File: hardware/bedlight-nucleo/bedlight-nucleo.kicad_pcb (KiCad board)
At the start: 2 copper layers, 76 x 76 mm, 18 parts, among them SW1 SW_Push, SW2 SW_Push, SW3 SW_Push, SW4 SW_Push, U1 Nucleo-32, U2 ULN2003A

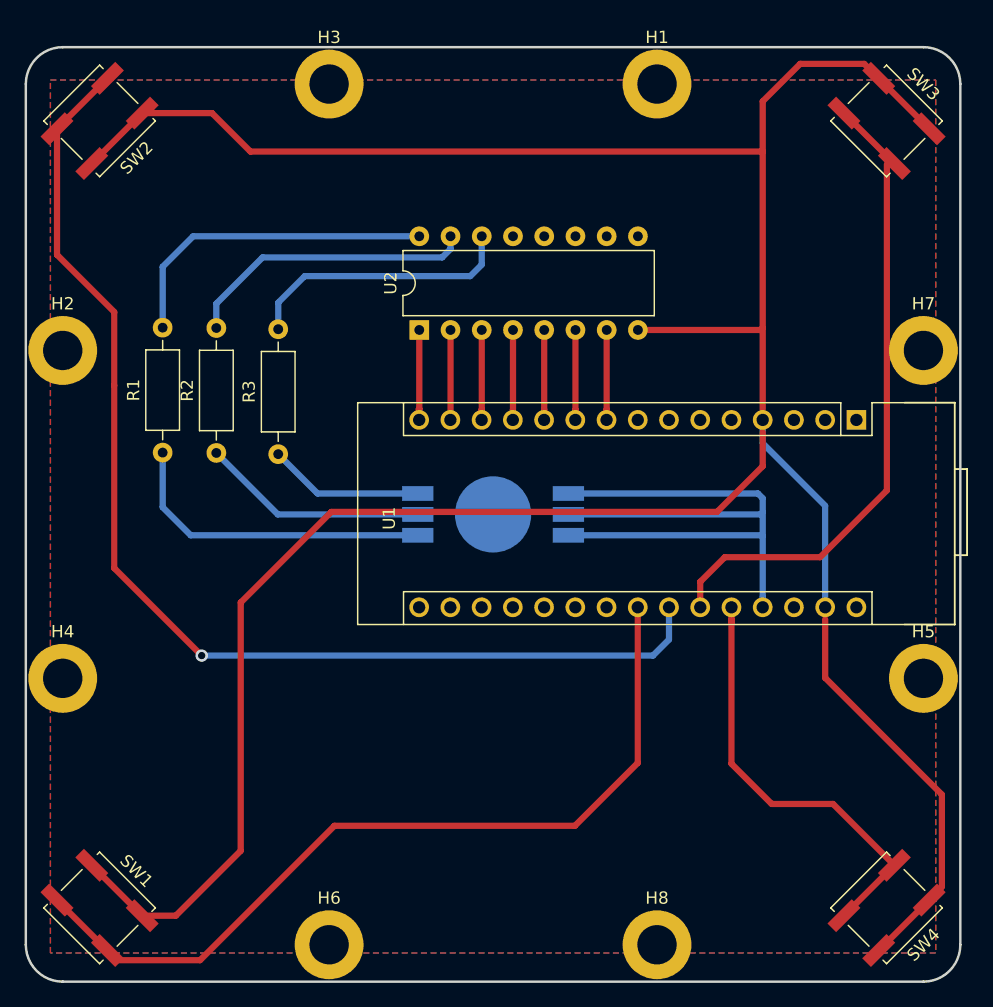
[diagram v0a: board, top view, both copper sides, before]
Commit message: Button footprints changed - ready for production
* Screw holes 3,2mm -> 3,3 mm
* Changed button footprint
* Enlarged copper fill on both sides
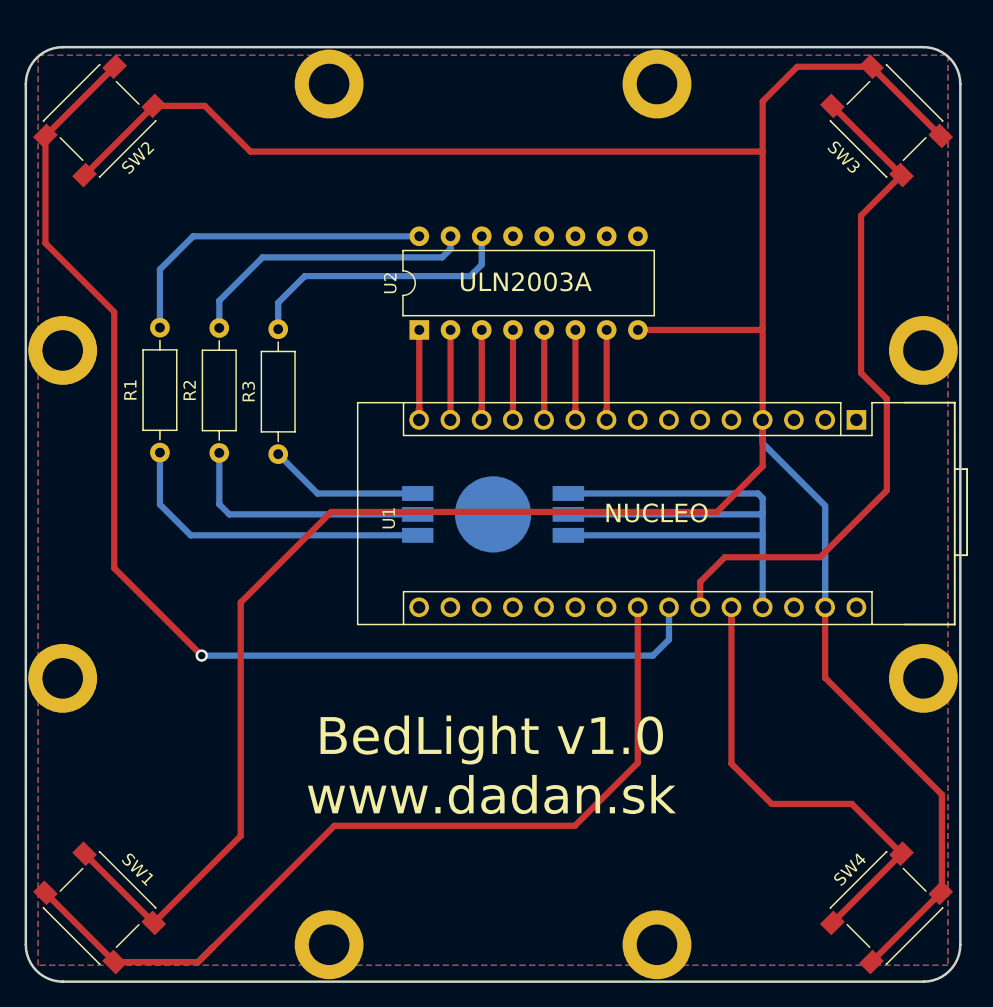
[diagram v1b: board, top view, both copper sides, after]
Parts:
- SW1, SW2, SW3, SW4: footprint Button_Switch_SMD:SW_Push_1P1T_NO_CK_KSC6xxJ -> Button_Switch_SMD:SW_SPST_PTS645
- moved R2 0.24 mm to (141.7, 107.3)
- moved R1 0.22 mm to (136.9, 107.3)
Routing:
- net GND: track 246.2 -> 252.8 mm
- net /BUTTON3: track 52.7 -> 56.2 mm
- net /BUTTON1: track 68.6 -> 71.3 mm
- net /BUTTON4: track 35.5 -> 37.8 mm
- net Net-(D1-Pad2): track 18.5 -> 20.7 mm
- net /BUTTON2: track 94.7 -> 96.7 mm
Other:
- board text added: "BedLight v1.0 www.dadan.sk"
- board text added: "NUCLEO"
- board text added: "ULN2003A"
